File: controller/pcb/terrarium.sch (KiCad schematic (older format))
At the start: 56 parts, among them K1 G3MB-202P, K2 G3MB-202P, K3 G3MB-202P, Q1 S8050, Q2 S8050, Q3 S8050, SW1 RST, U1 ESP32-WROOM-32, U2 DS3231M, U5 TCA9548APWR

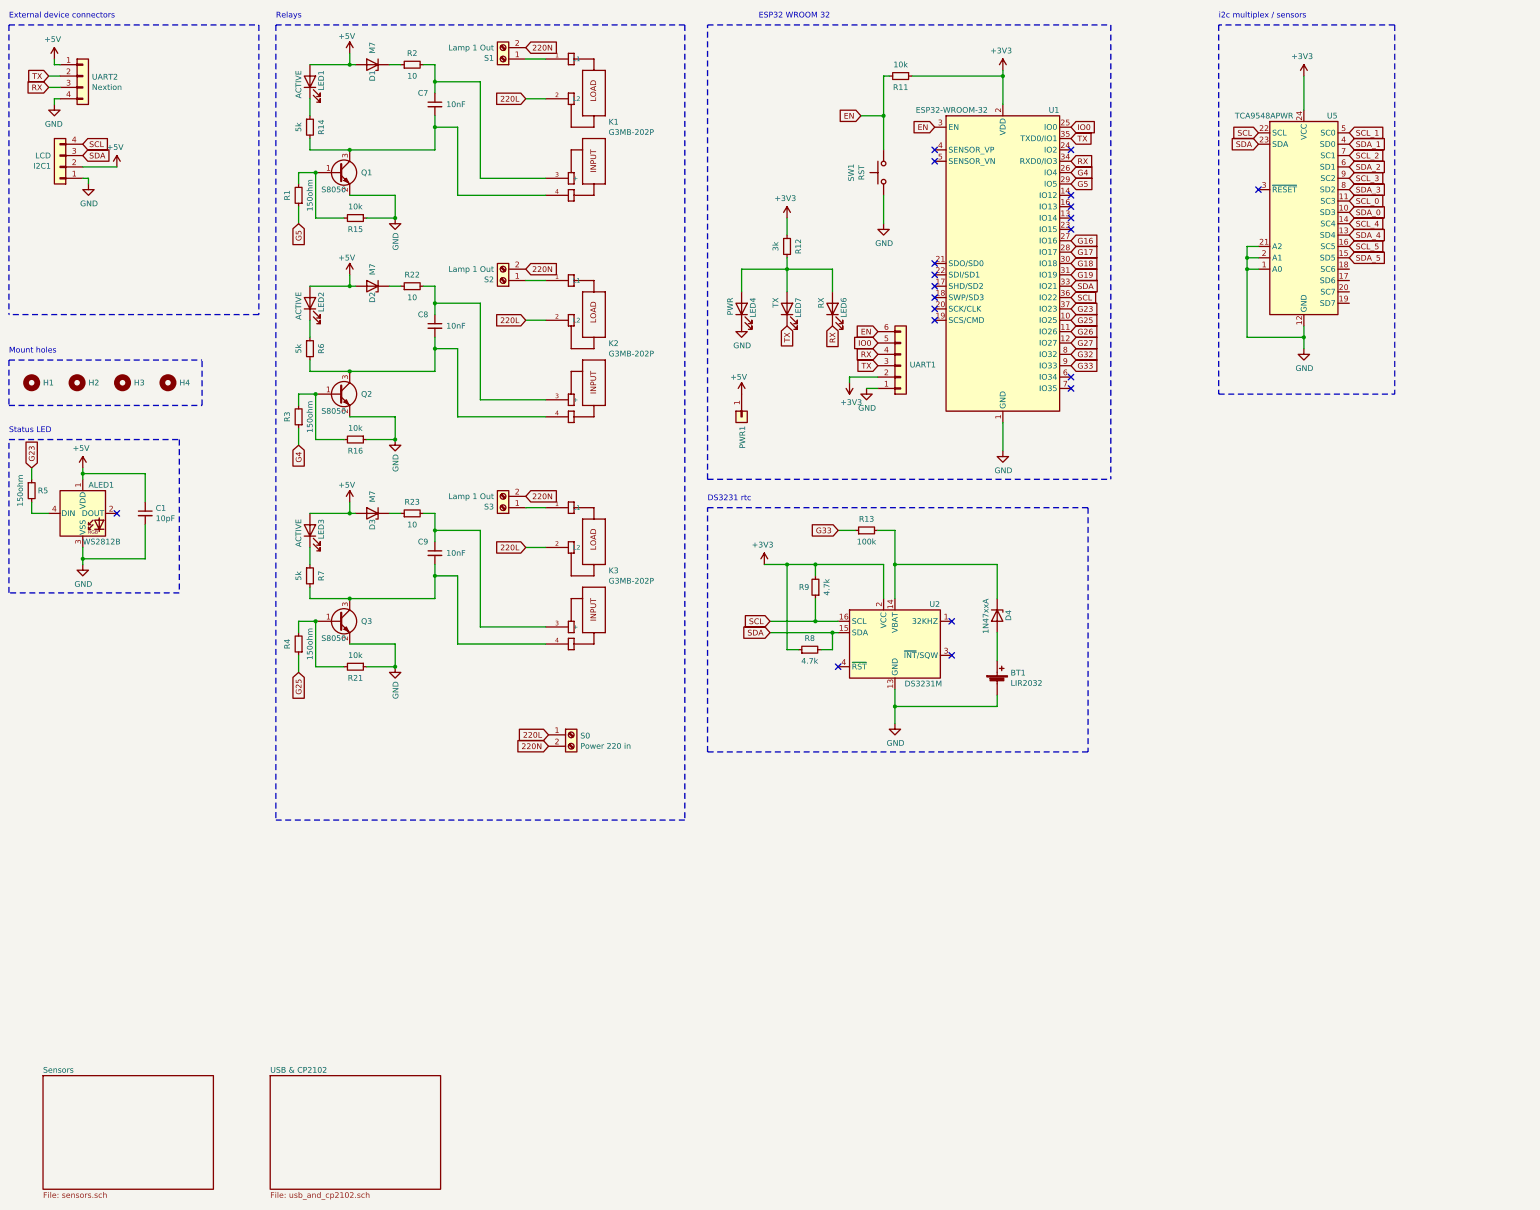
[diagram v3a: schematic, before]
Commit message: Controller pcb/v1.7 (#5)
* move components around

* pcb v1.7 done

Co-authored-by: Grigorii Merkushev <brushknight@pop-os.localdomain>
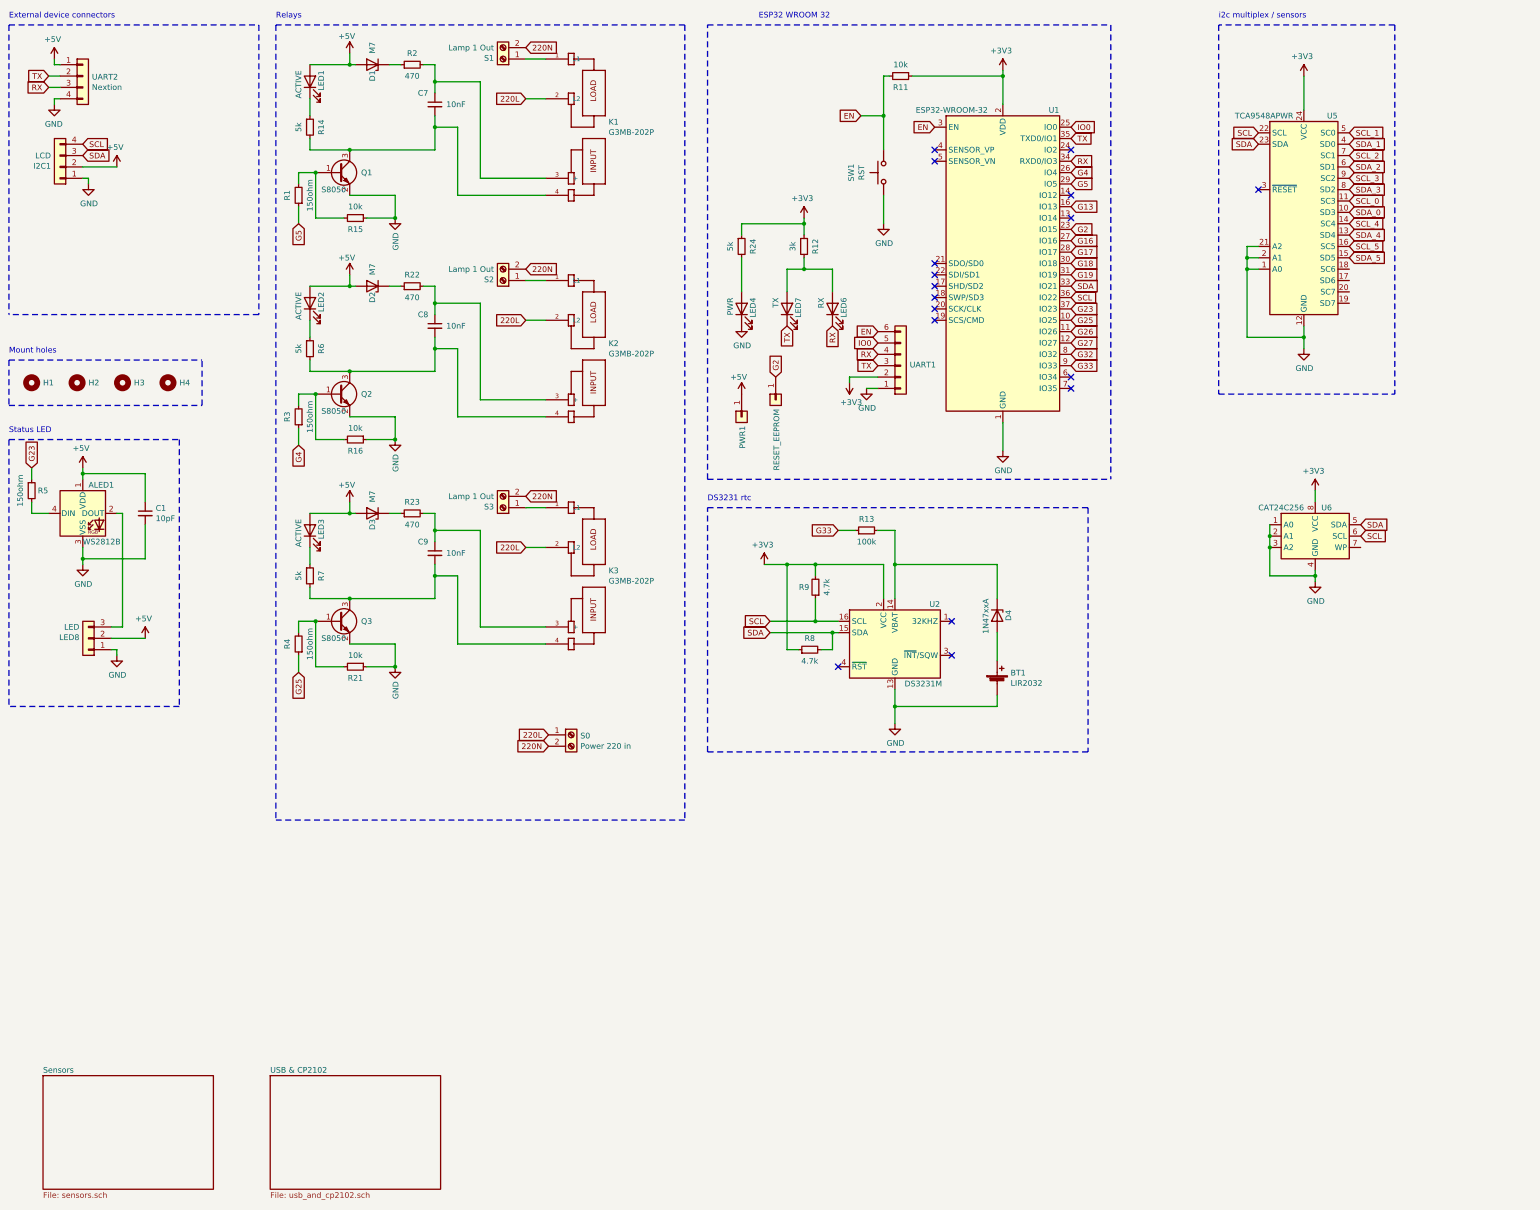
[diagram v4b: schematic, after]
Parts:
- added LED8: LED, Connector_JST:JST_XH_B3B-XH-A_1x03_P2.50mm_Vertical, symbol Connector_Generic:Conn_01x03
- added R24: 5k, Resistor_SMD:R_1206_3216Metric, symbol Device:R_Small
- added RESET_EEPROM: data, Connector_PinHeader_2.54mm:PinHeader_1x01_P2.54mm_Vertical, symbol Connector_Generic:Conn_01x01
- added U6: CAT24C256, Package_DIP:DIP-8_W7.62mm_Socket, symbol Memory_EEPROM:CAT24C256
- R2, R22, R23: value 10 -> 470
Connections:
- net +3V3: now also R24.1, U6.8 (VCC)
- net +5V: now also LED8.2 (Pin_2)
- net GND: now also LED8.1 (Pin_1), U6.1 (A0), U6.2 (A1), U6.3 (A2), U6.4 (GND)
- net SCL: now also U6.6 (SCL)
- net SDA: now also U6.5 (SDA)
- net at ALED1.2 (DOUT): now also LED8.3 (Pin_3)
- net G13: now reaches U1.16 (IO13)
- net G2: now reaches U1.23 (IO15)
- net G2: now also RESET_EEPROM.1 (Pin_1)
- net at LED6.2 (A), LED7.2 (A), R12.2: no longer LED4.2 (A)
- new net: LED4.2 (A), R24.2
- no-connect marks 20 -> 17
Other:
- moved on the sheet: R12
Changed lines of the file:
@@
 Text Notes 3050 650  0    50   ~ 0
 Relays
-Wire Notes Line
-	700  5700 700  4350
 Text Notes 700  4300 0    50   ~ 0
 Status LED
@@
 	1350 5300 1350 5400
 Connection ~ 1350 5400
-NoConn ~ 1650 5000
 $Comp
 L Device:R_Small R5
@@
 NoConn ~ 10050 1800
 NoConn ~ 10050 2200
-NoConn ~ 10050 2300
 NoConn ~ 10050 2400
-NoConn ~ 10050 2500
 NoConn ~ 10050 3800
 NoConn ~ 10050 3900
@@
 	700  4350 2200 4350
 Wire Notes Line
-	2200 4350 2200 5700
-Wire Notes Line
-	2200 5700 700  5700
+	2200 6700 700  6700
 Wire Notes Line
 	6850 4700 6850 700
@@
 L Device:R_Small R12
 U 1 1 624CEFE7
-P 7550 2650
-F 0 "R12" V 7650 2650 50  0000 C CNN
-F 1 "3k" V 7450 2650 50  0000 C CNN
-F 2 "Resistor_SMD:R_1206_3216Metric" H 7550 2650 50  0001 C CNN
-F 3 "~" H 7550 2650 50  0001 C CNN
-	1    7550 2650
-	1    0    0    -1
-$EndComp
-Wire Wire Line
-	7550 2750 7550 2850
-Wire Wire Line
-	7550 2400 7550 2550
+P 7700 2650
+F 0 "R12" V 7800 2650 50  0000 C CNN
+F 1 "3k" V 7600 2650 50  0000 C CNN
+F 2 "Resistor_SMD:R_1206_3216Metric" H 7700 2650 50  0001 C CNN
+F 3 "~" H 7700 2650 50  0001 C CNN
+	1    7700 2650
+	1    0    0    -1
+$EndComp
+Wire Wire Line
+	7700 2400 7700 2450
 $Comp
 L power:+3V3 #PWR0101
 U 1 1 61EFC8AF
-P 7550 2400
-F 0 "#PWR0101" H 7550 2250 50  0001 C CNN
-F 1 "+3V3" H 7565 2573 50  0000 C CNN
-F 2 "" H 7550 2400 50  0001 C CNN
-F 3 "" H 7550 2400 50  0001 C CNN
-	1    7550 2400
+P 7700 2400
+F 0 "#PWR0101" H 7700 2250 50  0001 C CNN
+F 1 "+3V3" H 7715 2573 50  0000 C CNN
+F 2 "" H 7700 2400 50  0001 C CNN
+F 3 "" H 7700 2400 50  0001 C CNN
+	1    7700 2400
 	-1   0    0    -1
 $EndComp
 Wire Wire Line
 	8500 5450 9400 5450
-Wire Wire Line
-	7550 2850 7150 2850
-Wire Wire Line
-	7150 2850 7150 3050
-Connection ~ 7550 2850
 $Comp
 L power:GND #PWR0102
@@
 $EndComp
 Wire Wire Line
-	7550 2850 7950 2850
+	7550 2850 7700 2850
 Wire Notes Line
 	700  3650 2400 3650
@@
 P 4250 1050
 F 0 "R2" V 4350 1050 50  0000 C CNN
-F 1 "10" V 4150 1050 50  0000 C CNN
+F 1 "470" V 4150 1050 50  0000 C CNN
 F 2 "Resistor_SMD:R_1206_3216Metric" H 4250 1050 50  0001 C CNN
 F 3 "~" H 4250 1050 50  0001 C CNN
@@
 P 4250 3000
 F 0 "R22" V 4350 3000 50  0000 C CNN
-F 1 "10" V 4150 3000 50  0000 C CNN
+F 1 "470" V 4150 3000 50  0000 C CNN
 F 2 "Resistor_SMD:R_1206_3216Metric" H 4250 3000 50  0001 C CNN
 F 3 "~" H 4250 3000 50  0001 C CNN
@@
 P 4250 5000
 F 0 "R23" V 4350 5000 50  0000 C CNN
-F 1 "10" V 4150 5000 50  0000 C CNN
+F 1 "470" V 4150 5000 50  0000 C CNN
 F 2 "Resistor_SMD:R_1206_3216Metric" H 4250 5000 50  0001 C CNN
 F 3 "~" H 4250 5000 50  0001 C CNN
@@
 	0    -1   -1   0
 $EndComp
+$Comp
+L Device:R_Small R24
+U 1 1 623FF425
+P 7150 2650
+F 0 "R24" V 7250 2650 50  0000 C CNN
+F 1 "5k" V 7050 2650 50  0000 C CNN
+F 2 "Resistor_SMD:R_1206_3216Metric" H 7150 2650 50  0001 C CNN
+F 3 "~" H 7150 2650 50  0001 C CNN
+	1    7150 2650
+	1    0    0    -1
+$EndComp
+Wire Wire Line
+	7150 2750 7150 3050
+Wire Wire Line
+	7700 2750 7700 2850
+Connection ~ 7700 2850
+Wire Wire Line
+	7700 2850 7950 2850
+Wire Wire Line
+	7150 2550 7150 2450
+Wire Wire Line
+	7150 2450 7700 2450
+Connection ~ 7700 2450
+Wire Wire Line
+	7700 2450 7700 2550
+Text GLabel 10050 2300 2    50   Input ~ 0
+G13
+$Comp
+L Memory_EEPROM:CAT24C256 U6
+U 1 1 629D9AE3
+P 12200 5200
+F 0 "U6" H 12300 5450 50  0000 C CNN
+F 1 "CAT24C256" H 11900 5450 50  0000 C CNN
+F 2 "Package_DIP:DIP-8_W7.62mm_Socket" H 12200 5200 50  0001 C CNN
+F 3 "https://www.onsemi.cn/PowerSolutions/document/CAT24C256-D.PDF" H 12200 5200 50  0001 C CNN
+	1    12200 5200
+	1    0    0    -1
+$EndComp
+Text GLabel 12600 5100 2    50   Input ~ 0
+SDA
+Text GLabel 12600 5200 2    50   Input ~ 0
+SCL
+$Comp
+L power:GND #PWR0103
+U 1 1 629E21BF
+P 12200 5600
+F 0 "#PWR0103" H 12200 5350 50  0001 C CNN
+F 1 "GND" H 12205 5427 50  0000 C CNN
+F 2 "" H 12200 5600 50  0001 C CNN
+F 3 "" H 12200 5600 50  0001 C CNN
+	1    12200 5600
+	1    0    0    -1
+$EndComp
+Wire Wire Line
+	12200 5600 12200 5550
+Wire Wire Line
+	12200 5550 11800 5550
+Wire Wire Line
+	11800 5550 11800 5300
+Connection ~ 12200 5550
+Wire Wire Line
+	12200 5550 12200 5500
+Connection ~ 11800 5200
+Wire Wire Line
+	11800 5200 11800 5100
+Connection ~ 11800 5300
+Wire Wire Line
+	11800 5300 11800 5200
+$Comp
+L power:+3V3 #PWR0104
+U 1 1 629FC42C
+P 12200 4800
+F 0 "#PWR0104" H 12200 4650 50  0001 C CNN
+F 1 "+3V3" H 12215 4973 50  0000 C CNN
+F 2 "" H 12200 4800 50  0001 C CNN
+F 3 "" H 12200 4800 50  0001 C CNN
+	1    12200 4800
+	-1   0    0    -1
+$EndComp
+Wire Wire Line
+	12200 4800 12200 4900
+$Comp
+L Connector_Generic:Conn_01x03 LED8
+U 1 1 62B28163
+P 1400 6100
+F 0 "LED8" H 1480 6092 50  0000 L CNN
+F 1 "LED" H 1480 6001 50  0000 L CNN
+F 2 "Connector_JST:JST_XH_B3B-XH-A_1x03_P2.50mm_Vertical" H 1400 6100 50  0001 C CNN
+F 3 "~" H 1400 6100 50  0001 C CNN
+	1    1400 6100
+	-1   0    0    1
+$EndComp
+$Comp
+L power:GND #PWR020
+U 1 1 62B2816B
+P 1650 6250
+F 0 "#PWR020" H 1650 6000 50  0001 C CNN
+F 1 "GND" H 1655 6077 50  0000 C CNN
+F 2 "" H 1650 6250 50  0001 C CNN
+F 3 "" H 1650 6250 50  0001 C CNN
+	1    1650 6250
+	1    0    0    -1
+$EndComp
+Wire Wire Line
+	1650 6250 1650 6200
+Wire Wire Line
+	1650 6200 1600 6200
+$Comp
+L power:+5V #PWR021
+U 1 1 62B28173
+P 1900 6100
+F 0 "#PWR021" H 1900 5950 50  0001 C CNN
+F 1 "+5V" H 1915 6273 50  0000 C CNN
+F 2 "" H 1900 6100 50  0001 C CNN
+F 3 "" H 1900 6100 50  0001 C CNN
+	1    1900 6100
+	-1   0    0    -1
+$EndComp
+Wire Wire Line
+	1900 6100 1600 6100
+Wire Notes Line
+	2200 4350 2200 6700
+Wire Notes Line
+	700  4350 700  6700
+Wire Wire Line
+	1650 5000 1700 5000
+Wire Wire Line
+	1700 5000 1700 6000
+Wire Wire Line
+	1700 6000 1600 6000
+$Comp
+L Connector_Generic:Conn_01x01 RESET_EEPROM
+U 1 1 62BA3F8C
+P 7450 4000
+F 0 "RESET_EEPROM" H 7530 3992 50  0000 L CNN
+F 1 "data" H 7600 3400 50  0001 L CNN
+F 2 "Connector_PinHeader_2.54mm:PinHeader_1x01_P2.54mm_Vertical" H 7450 4000 50  0001 C CNN
+F 3 "~" H 7450 4000 50  0001 C CNN
+	1    7450 4000
+	0    -1   1    0
+$EndComp
+Text GLabel 7450 3800 1    50   Input ~ 0
+G2
+Text GLabel 10050 2500 2    50   Input ~ 0
+G2
 $EndSCHEMATC
